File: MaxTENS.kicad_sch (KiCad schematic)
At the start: 19 parts, among them J2 PJ-040-SMT-TR, J6 Conn_01x02_Pin, J7 PJ-040-SMT-TR

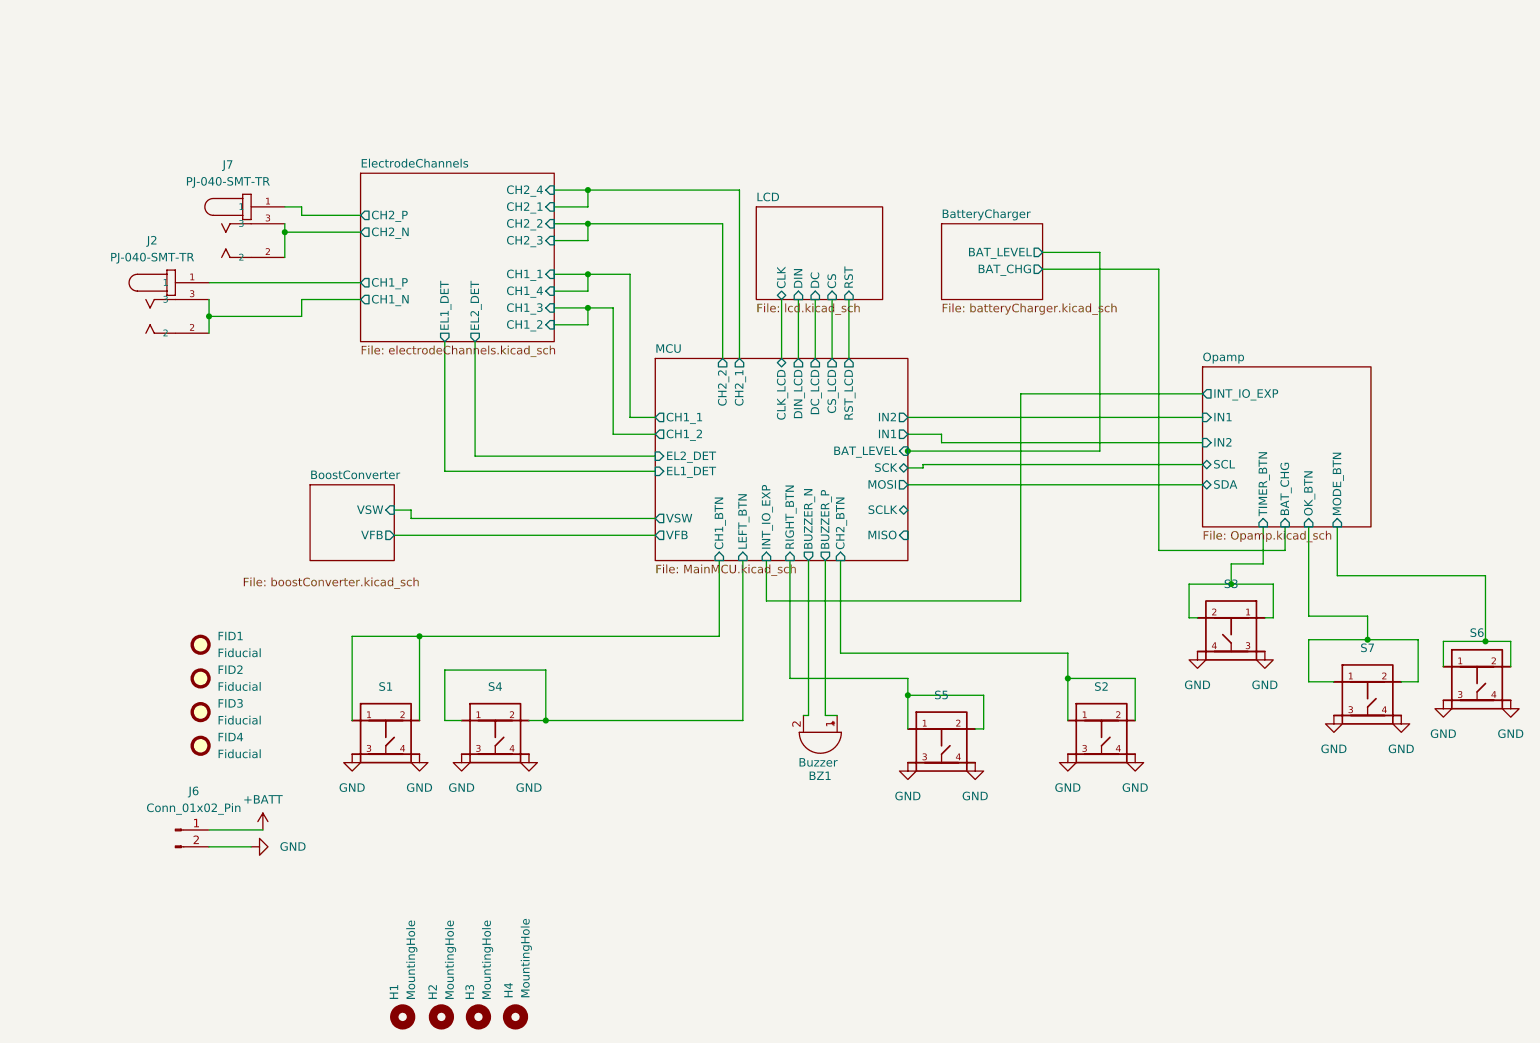
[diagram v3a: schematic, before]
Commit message: version 5: replaced ESP32-WROVER module with ESP-Mini, removed 2.5mm plugs, changed USB connector and routed electrode signals on it, added RC snubber circuit to boost converter and output caps to reduce switching loop
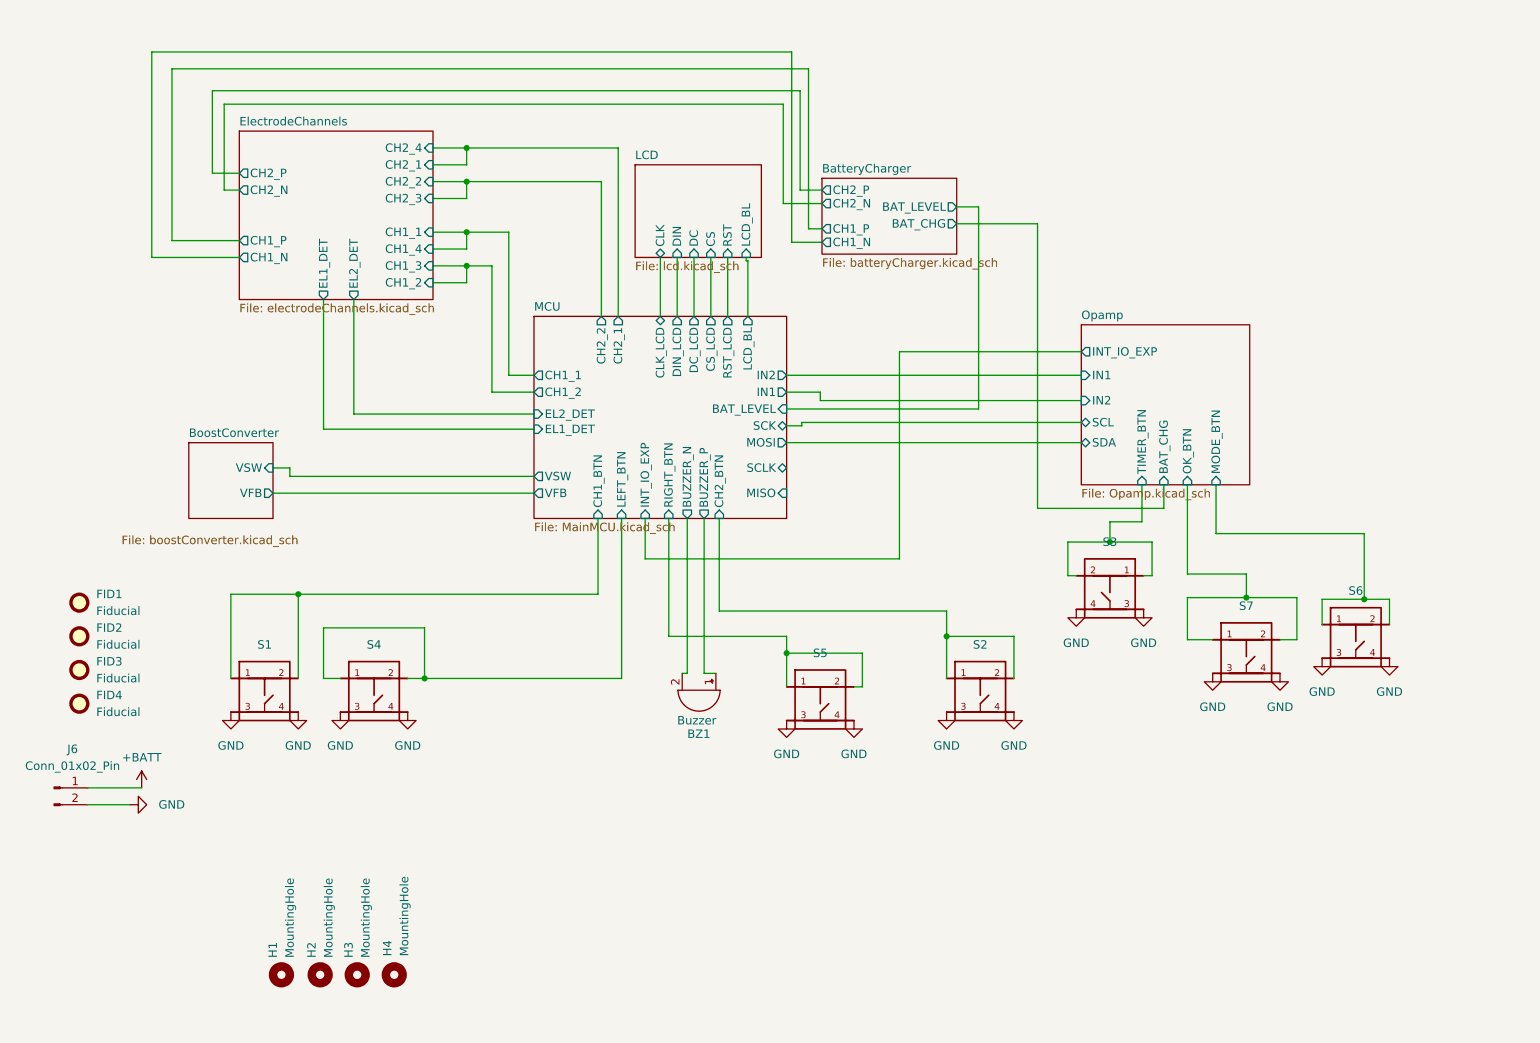
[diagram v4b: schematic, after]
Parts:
- removed J2, J7: PJ-040-SMT-TR, Library:CUI_PJ-040-SMT-TR, symbol 2023-09-03_14-36-57:PJ-040-SMT-TR
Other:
- sheet BatteryCharger ports: added CH1_N, CH1_P, CH2_N, CH2_P; removed none
- sheet LCD ports: added LCD_BL; removed none
- sheet MCU ports: added LCD_BL; removed none
- moved on the sheet: BZ1, FID1, FID2, FID3, FID4, H1, H2, H3, H4, J6, S1, S2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

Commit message: Fixed electrode detection mechanism, modified position of USB Type-C port
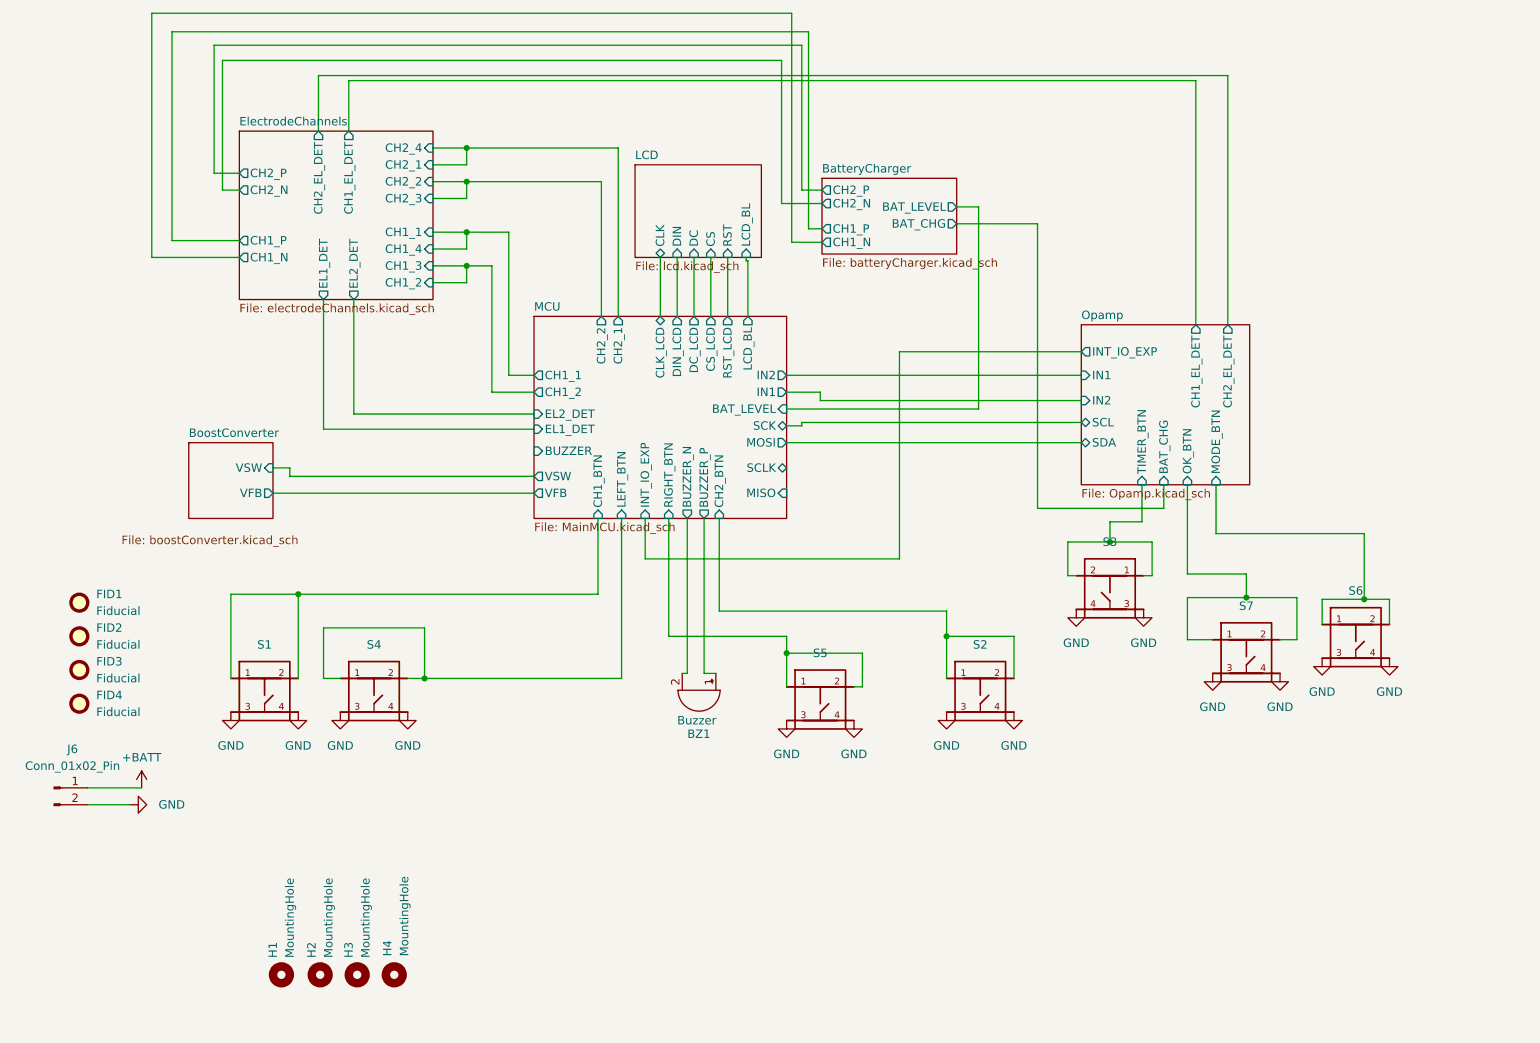
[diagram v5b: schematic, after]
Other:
- sheet ElectrodeChannels ports: added CH1_EL_DET, CH2_EL_DET; removed none
- sheet MCU ports: added BUZZER; removed none
- sheet Opamp ports: added CH1_EL_DET, CH2_EL_DET; removed none
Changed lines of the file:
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@@
+    (stroke (width 0) (type default))
+  )
+  (wire (pts (xy 97.79 28.448) (xy 234.95 28.448))
     (stroke (width 0) (type default))
   )
@@
     (stroke (width 0) (type default))
   )
-  (wire (pts (xy 167.894 47.752) (xy 167.894 32.766))
+  (wire (pts (xy 167.64 47.752) (xy 167.64 26.162))
     (stroke (width 0) (type default))
   )
@@
     (stroke (width 0) (type default))
   )
+  (wire (pts (xy 97.79 36.83) (xy 97.79 28.448))
+    (stroke (width 0) (type default))
+  )
   (wire (pts (xy 120.142 41.91) (xy 120.142 39.37))
     (stroke (width 0) (type default))
@@
     (stroke (width 0) (type default))
   )
+  (wire (pts (xy 102.362 29.21) (xy 102.362 36.83))
+    (stroke (width 0) (type default))
+  )
   (wire (pts (xy 245.364 107.188) (xy 245.364 113.538))
     (stroke (width 0) (type default))
@@
     (stroke (width 0) (type default))
   )
-  (wire (pts (xy 75.692 27.432) (xy 171.704 27.432))
+  (wire (pts (xy 75.692 21.844) (xy 171.704 21.844))
     (stroke (width 0) (type default))
   )
@@
     (stroke (width 0) (type default))
   )
-  (wire (pts (xy 169.164 24.892) (xy 72.644 24.892))
+  (wire (pts (xy 169.164 19.05) (xy 72.644 19.05))
     (stroke (width 0) (type default))
   )
@@
     (stroke (width 0) (type default))
   )
+  (wire (pts (xy 230.124 29.21) (xy 230.124 66.04))
+    (stroke (width 0) (type default))
+  )
   (wire (pts (xy 228.854 107.188) (xy 237.744 107.188))
     (stroke (width 0) (type default))
@@
     (stroke (width 0) (type default))
   )
+  (wire (pts (xy 234.95 28.448) (xy 234.95 66.04))
+    (stroke (width 0) (type default))
+  )
   (wire (pts (xy 84.582 106.68) (xy 94.742 106.68))
     (stroke (width 0) (type default))
@@
     (stroke (width 0) (type default))
   )
+  (wire (pts (xy 102.362 29.21) (xy 230.124 29.21))
+    (stroke (width 0) (type default))
+  )
   (wire (pts (xy 223.52 103.886) (xy 222.25 103.886))
     (stroke (width 0) (type default))
@@
     (stroke (width 0) (type default))
   )
-  (wire (pts (xy 81.788 30.734) (xy 81.788 43.18))
+  (wire (pts (xy 82.042 23.876) (xy 82.042 43.18))
     (stroke (width 0) (type default))
   )
@@
     (stroke (width 0) (type default))
   )
-  (wire (pts (xy 171.704 27.432) (xy 171.704 51.562))
+  (wire (pts (xy 171.704 21.844) (xy 171.704 51.562))
     (stroke (width 0) (type default))
   )
@@
     (stroke (width 0) (type default))
   )
-  (wire (pts (xy 75.692 53.34) (xy 75.692 27.432))
-    (stroke (width 0) (type default))
-  )
-  (wire (pts (xy 169.164 53.594) (xy 169.164 24.892))
-    (stroke (width 0) (type default))
-  )
-  (wire (pts (xy 83.566 45.72) (xy 85.852 45.72))
+  (wire (pts (xy 75.692 53.34) (xy 75.692 21.844))
+    (stroke (width 0) (type default))
+  )
+  (wire (pts (xy 169.164 53.594) (xy 169.164 19.05))
+    (stroke (width 0) (type default))
+  )
+  (wire (pts (xy 83.312 45.72) (xy 85.852 45.72))
     (stroke (width 0) (type default))
   )
@@
     (stroke (width 0) (type default))
   )
-  (wire (pts (xy 173.736 45.72) (xy 170.434 45.72))
+  (wire (pts (xy 173.736 45.72) (xy 170.688 45.72))
     (stroke (width 0) (type default))
   )
@@
     (stroke (width 0) (type default))
   )
-  (wire (pts (xy 72.644 24.892) (xy 72.644 55.88))
+  (wire (pts (xy 72.644 19.05) (xy 72.644 55.88))
     (stroke (width 0) (type default))
   )
@@
     (stroke (width 0) (type default))
   )
-  (wire (pts (xy 170.434 45.72) (xy 170.434 30.734))
+  (wire (pts (xy 170.688 45.72) (xy 170.688 23.876))
     (stroke (width 0) (type default))
   )
@@
     (stroke (width 0) (type default))
   )
-  (wire (pts (xy 170.434 30.734) (xy 81.788 30.734))
+  (wire (pts (xy 170.688 23.876) (xy 82.042 23.876))
     (stroke (width 0) (type default))
   )
@@
     (stroke (width 0) (type default))
   )
-  (wire (pts (xy 81.788 43.18) (xy 85.852 43.18))
-    (stroke (width 0) (type default))
-  )
-  (wire (pts (xy 173.736 47.752) (xy 167.894 47.752))
+  (wire (pts (xy 82.042 43.18) (xy 85.852 43.18))
+    (stroke (width 0) (type default))
+  )
+  (wire (pts (xy 173.736 47.752) (xy 167.64 47.752))
     (stroke (width 0) (type default))
   )
@@
     (stroke (width 0) (type default))
   )
-  (wire (pts (xy 167.894 32.766) (xy 83.566 32.766))
+  (wire (pts (xy 167.64 26.162) (xy 83.312 26.162))
     (stroke (width 0) (type default))
   )
@@
     (stroke (width 0) (type default))
   )
-  (wire (pts (xy 83.566 32.766) (xy 83.566 45.72))
+  (wire (pts (xy 83.312 26.162) (xy 83.312 45.72))
     (stroke (width 0) (type default))
   )
@@
       (effects (font (size 1.27 1.27)) (justify left))
     )
+    (pin "CH2_EL_DET" output (at 97.79 36.83 90)
+      (effects (font (size 1.27 1.27)) (justify right))
+    )
+    (pin "CH1_EL_DET" output (at 102.362 36.83 90)
+      (effects (font (size 1.27 1.27)) (justify right))
+    )
     (instances
       (project "MaxTENS"
@@
       (effects (font (size 1.27 1.27)) (justify left))
     )
+    (pin "CH1_EL_DET" output (at 230.124 66.04 90)
+      (effects (font (size 1.27 1.27)) (justify right))
+    )
+    (pin "CH2_EL_DET" output (at 234.95 66.04 90)
+      (effects (font (size 1.27 1.27)) (justify right))
+    )
     (instances
       (project "MaxTENS"
@@
       (effects (font (size 1.27 1.27)) (justify right))
     )
-    (instances
+    (pin "BUZZER" input (at 130.302 85.09 180)
+      (effects (font (size 1.27 1.27)) (justify left))
+    )
+    (instances
